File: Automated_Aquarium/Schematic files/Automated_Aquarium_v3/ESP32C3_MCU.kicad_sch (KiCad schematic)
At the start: 11 parts, among them U1 ESP32-C3-MINI-1

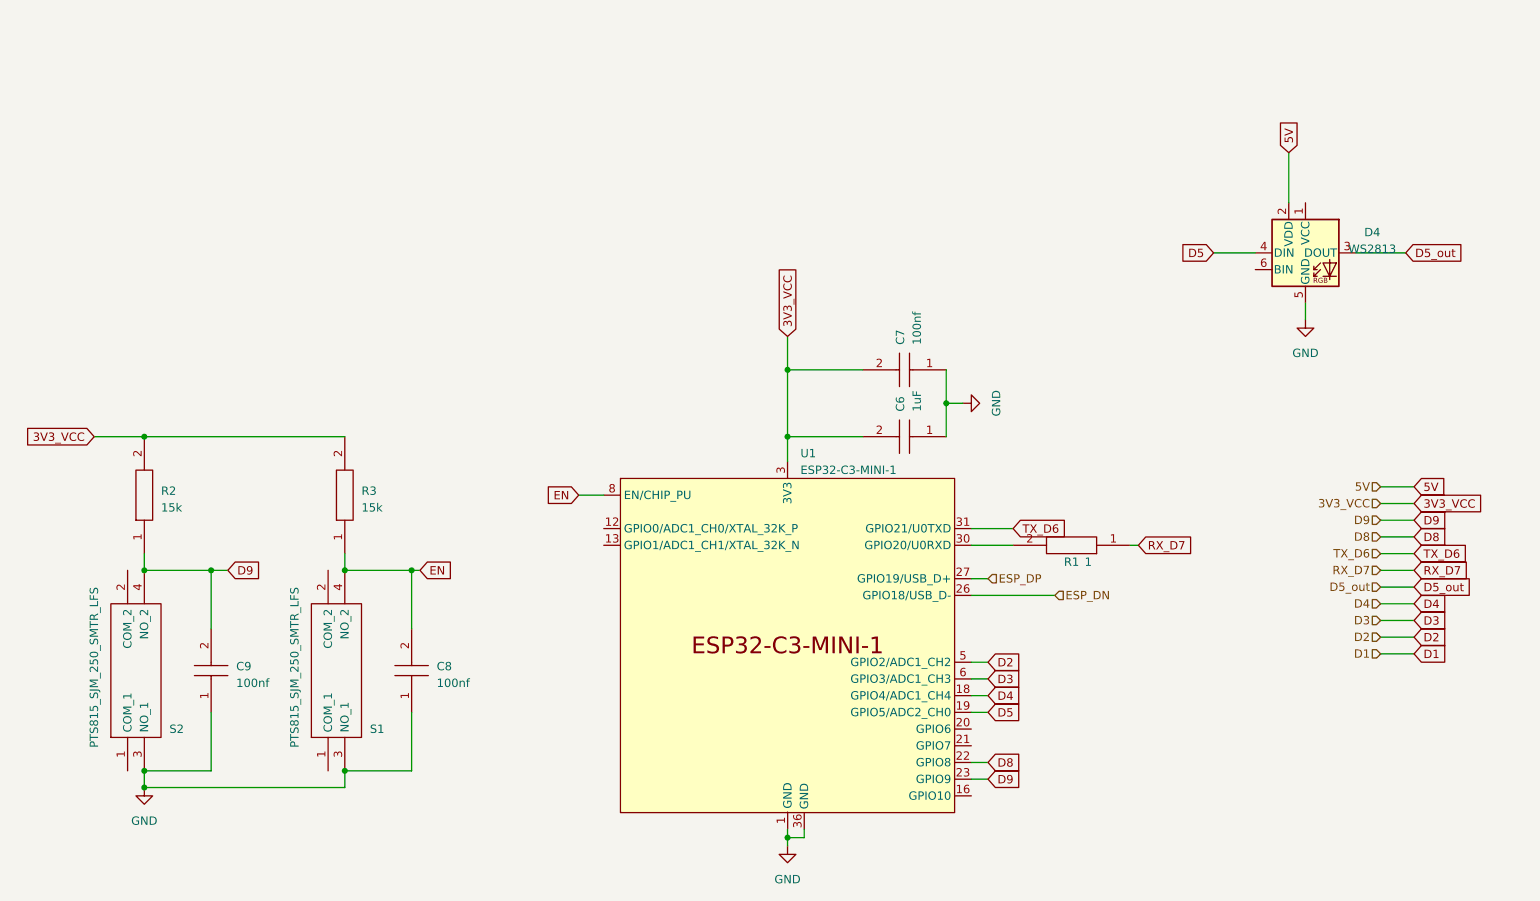
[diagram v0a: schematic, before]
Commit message: complete 0v1 layout aquarium
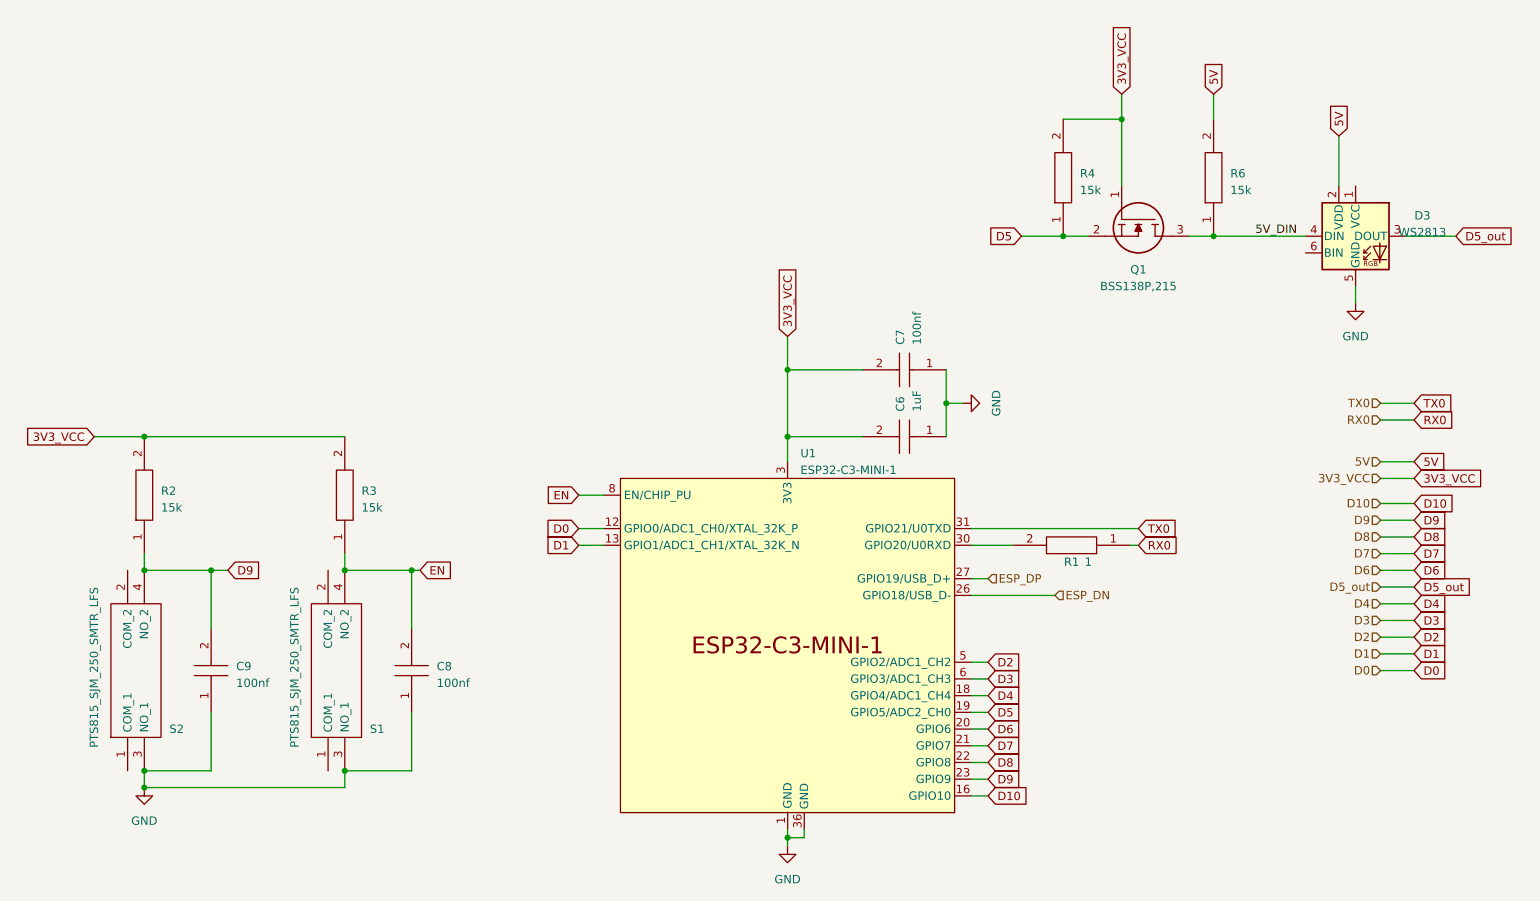
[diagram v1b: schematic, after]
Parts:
- removed D4: WS2813, LED_SMD:LED_WS2812_PLCC6_5.0x5.0mm_P1.6mm, symbol LED:WS2813
- added D3: WS2813, LED_SMD:LED_WS2812_PLCC6_5.0x5.0mm_P1.6mm, symbol LED:WS2813
- added Q1: BSS138P,215, SamacSys_Parts:SOT95P230X110-3N, symbol SamacSys_Parts:BSS138P,215
- added R4, R6: 15k, RESC1608X55N, symbol SamacSys_Parts:RMCF0603ZT0R00
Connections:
- net 3V3_VCC: now also Q1.1, R4.2
- net 5V: now also D3.2 (VDD), R6.2
- net D1: now also U1.13 (GPIO1/ADC1_CH1/XTAL_32K_N)
- net D5: now also Q1.2, R4.1
- net D5_out: now also D3.3 (DOUT)
- net GND: now also D3.5 (GND)
- net D0: now reaches U1.12 (GPIO0/ADC1_CH0/XTAL_32K_P)
- net D10: now reaches U1.16 (GPIO10)
- net D6: now reaches U1.20 (GPIO6)
- net D7: now reaches U1.21 (GPIO7)
- net RX_D7 renamed RX0
- net TX_D6 renamed TX0
- new net 5V_DIN: D3.4 (DIN), Q1.3, R6.1

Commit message: init pcb
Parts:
- S1, S2: footprint PTS815SJM250SMTRLFS -> SamacSys_Parts:PTS815SJM250SMTRLFS
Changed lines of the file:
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@@
       (effects (font (size 1.27 1.27)) (justify right))
     )
-    (property "Footprint" "PTS815SJM250SMTRLFS" (at 59.69 123.19 0)
+    (property "Footprint" "SamacSys_Parts:PTS815SJM250SMTRLFS" (at 59.69 123.19 0)
       (effects (font (size 1.27 1.27)) (justify left) hide)
     )
@@
       (effects (font (size 1.27 1.27)) (justify right))
     )
-    (property "Footprint" "PTS815SJM250SMTRLFS" (at 29.21 123.19 0)
-      (effects (font (size 1.27 1.27)) (justify left) hide)
-    )
+    (property "Footprint" "SamacSys_Parts:PTS815SJM250SMTRLFS" (at 29.21 123.19 0)
+      (effects (font (size 1.27 1.27)) (justify left) hide)
+    )

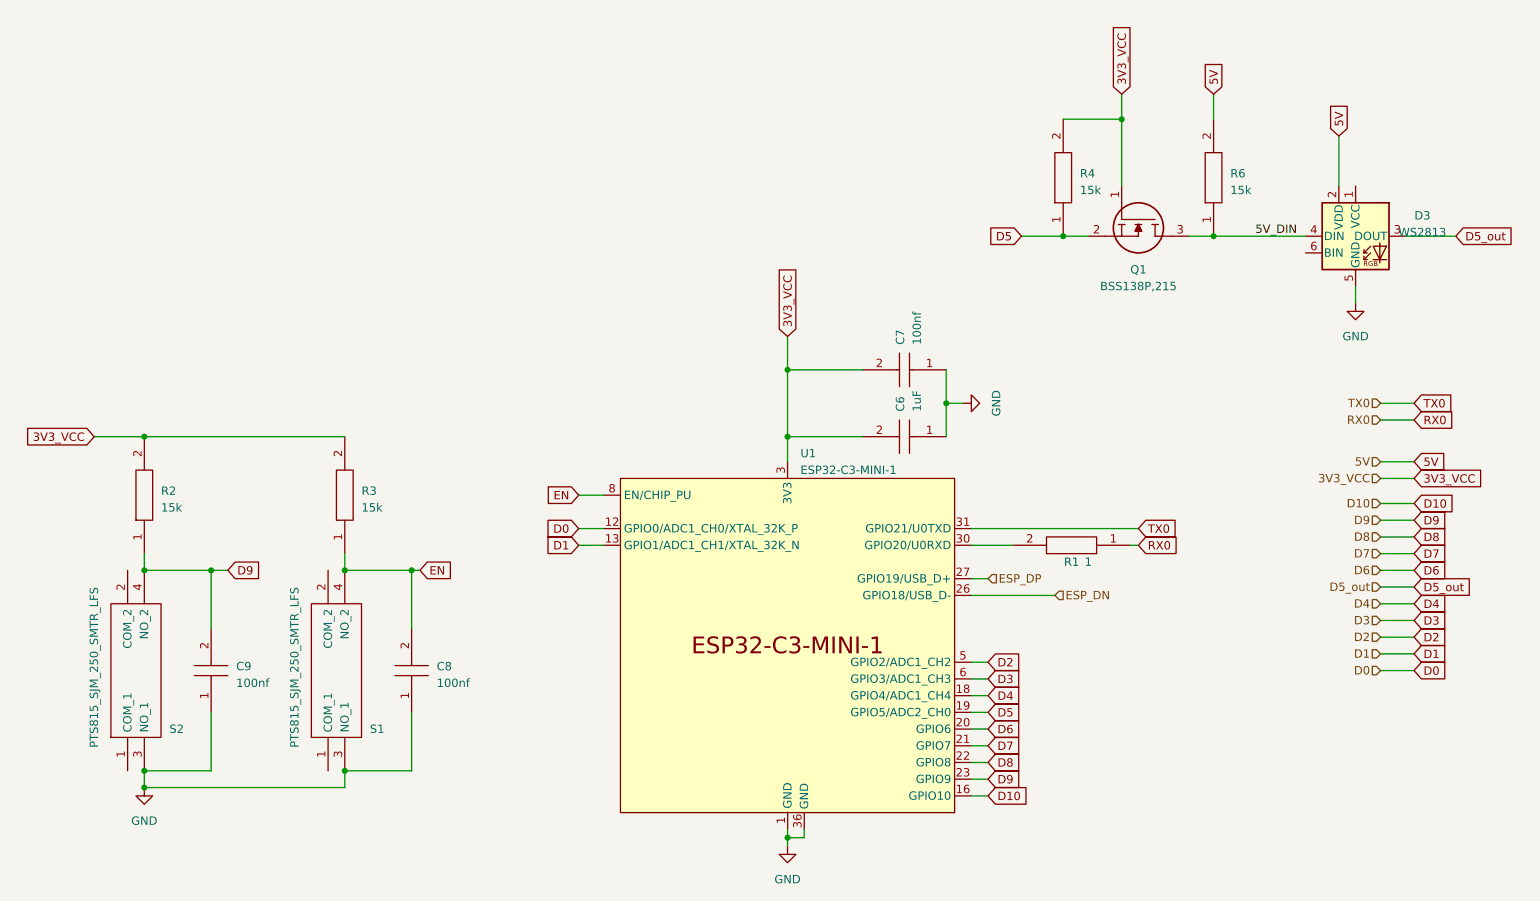
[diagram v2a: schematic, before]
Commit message: finish aqua schem, add inital layout
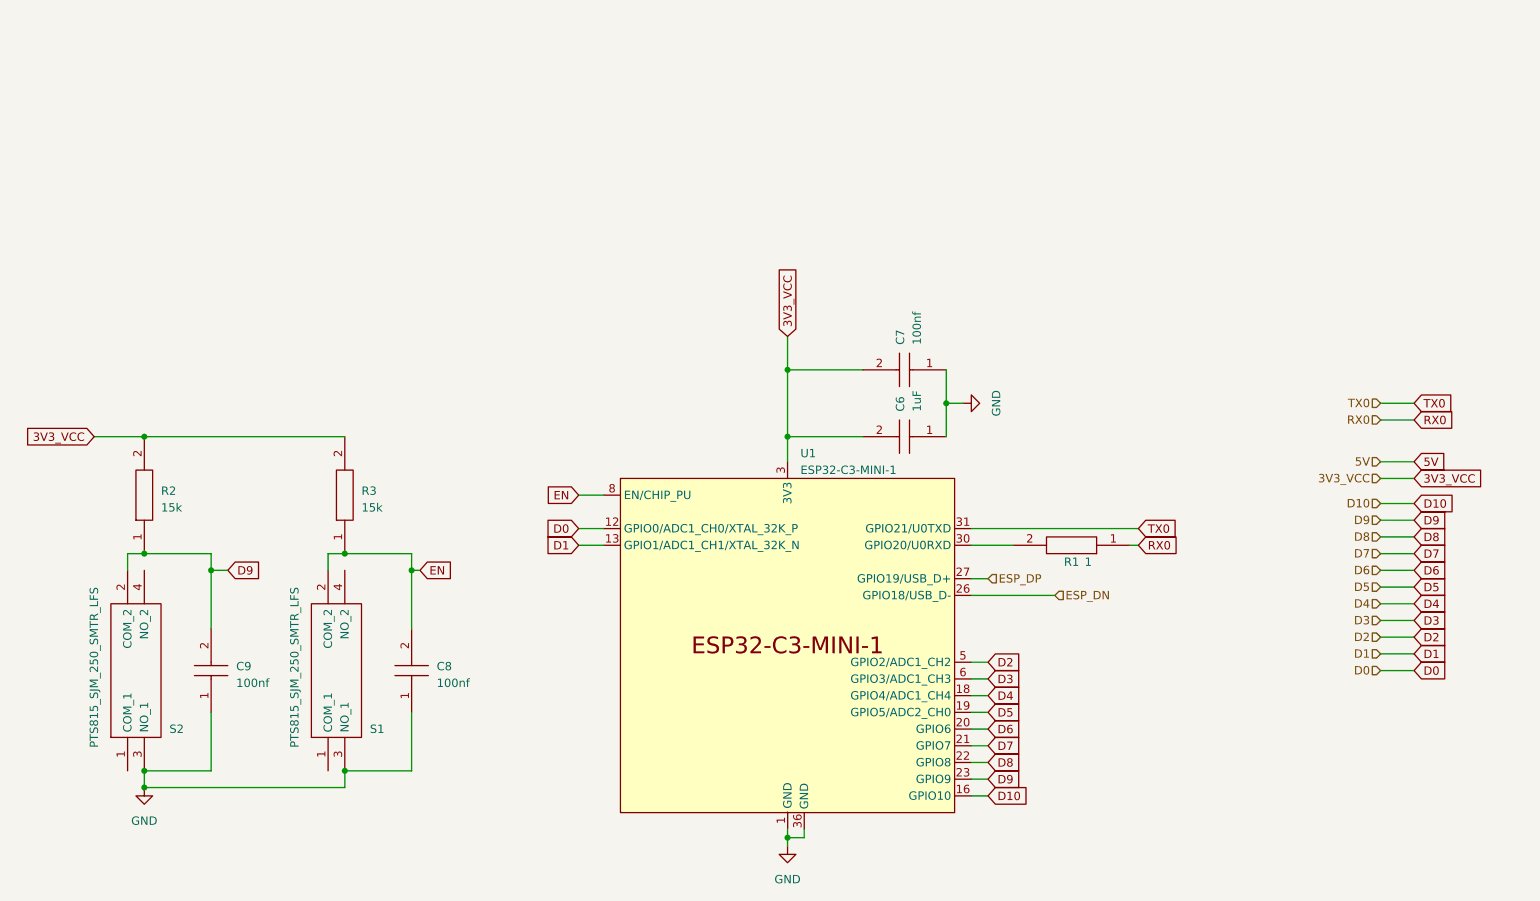
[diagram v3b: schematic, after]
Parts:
- removed D3: WS2813, LED_SMD:LED_WS2812_PLCC6_5.0x5.0mm_P1.6mm, symbol LED:WS2813
- removed Q1: BSS138P,215, SamacSys_Parts:SOT95P230X110-3N, symbol SamacSys_Parts:BSS138P,215
- removed R4, R6: 15k, RESC1608X55N, symbol SamacSys_Parts:RMCF0603ZT0R00
- C6: LCSC Part Number (none) -> C377755
- C7, C8, C9: LCSC Part Number (none) -> C307349
- R1: LCSC Part Number (none) -> C22936
- R2, R3: LCSC Part Number (none) -> C855633
- S1, S2: LCSC Part Number (none) -> C2689510
- U1: LCSC Part Number (none) -> C2934569
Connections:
- net D9: now also S2.2 (COM_2); no longer S2.4 (NO_2)
- net EN: now also S1.2 (COM_2); no longer S1.4 (NO_2)
